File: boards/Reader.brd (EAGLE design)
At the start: 107.6 x 88.9 mm, 46 parts, among them IC1 PIC18F4550_40, T1 BC547, T2 BC547, T3 BC547, X3 PN61729-S

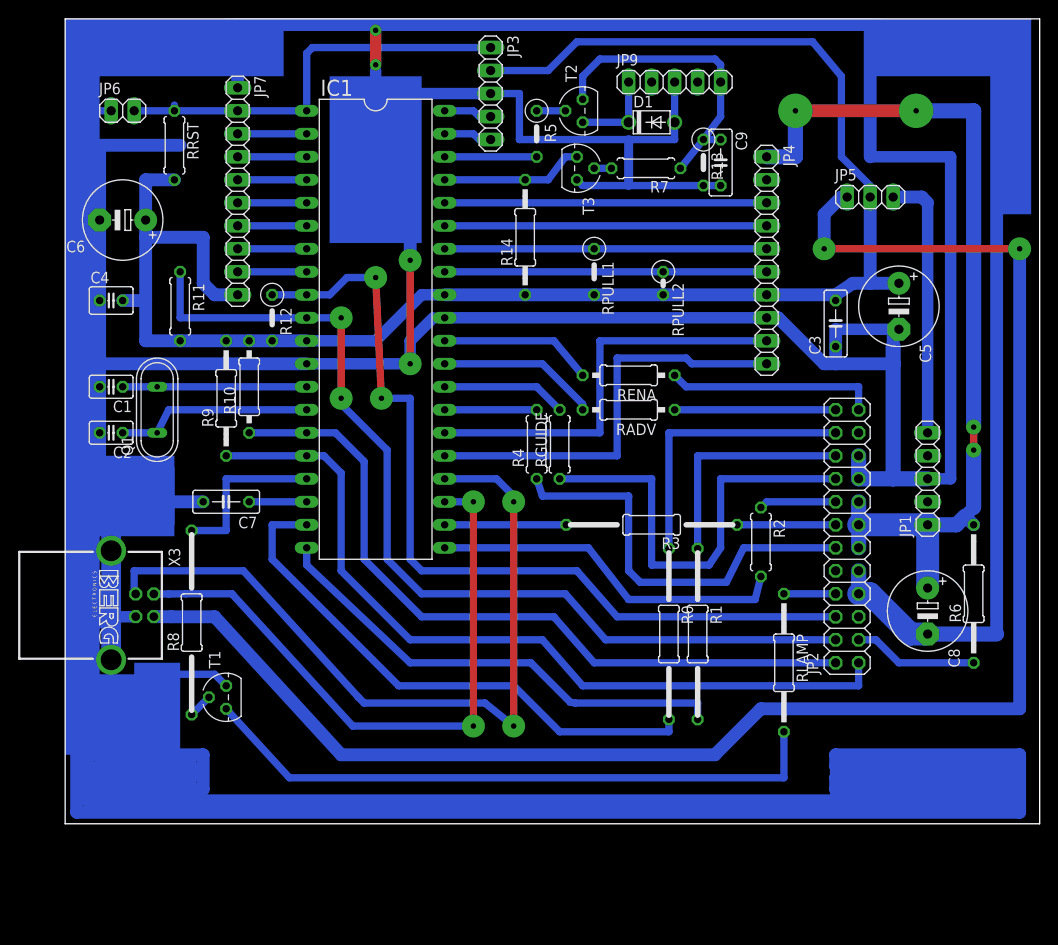
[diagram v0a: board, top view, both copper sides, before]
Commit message: Reader: Added new service
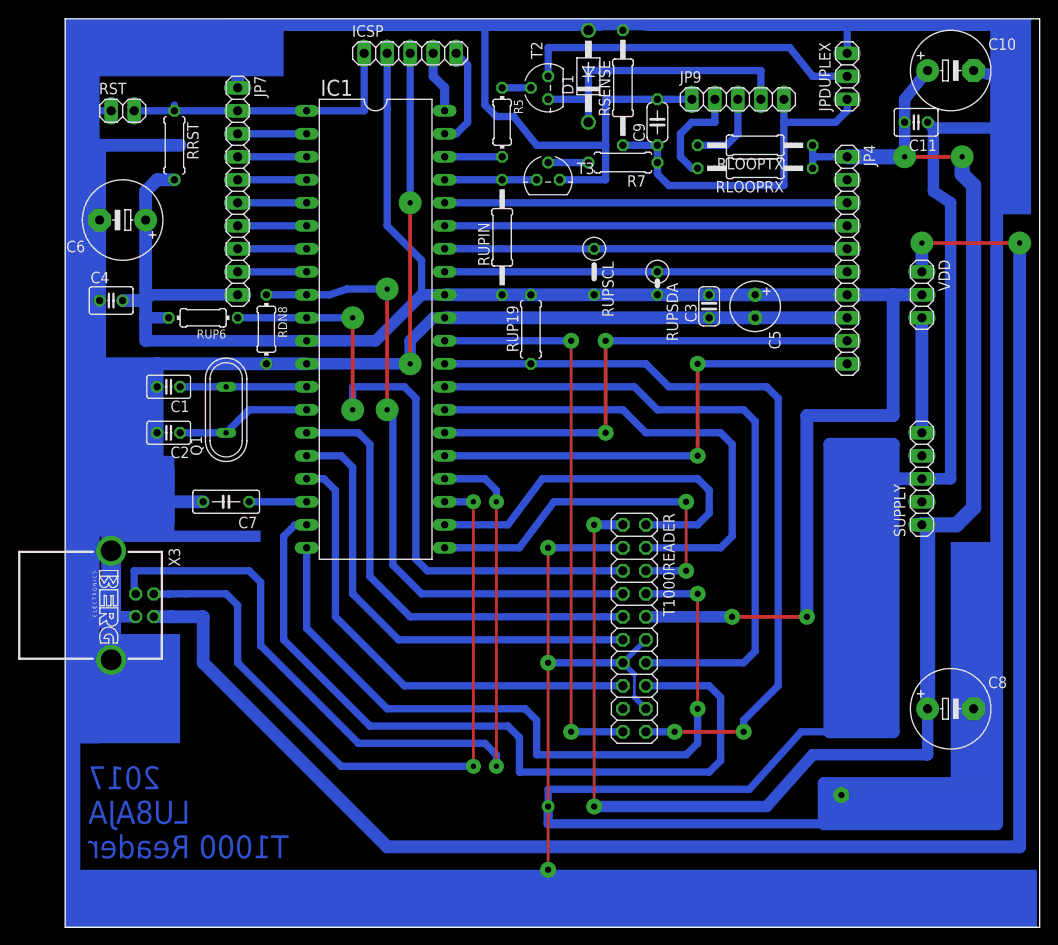
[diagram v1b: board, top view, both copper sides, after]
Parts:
- removed JP1, JP3: (no value), pinhead:1X05
- removed JP2: (no value), pinhead:2X12
- removed JP5: (no value), pinhead:1X03
- removed R0, R1, R3: R-EU0207/19, custom:0207/19
- removed R10, RADV, RENA: R-EU0207/10, custom:0207/10
- removed R11, R2, R4, RGUIDE: R-EU0207/7, custom:0207/7
- removed R12, R13: R-EU0207/5V, custom:0207/5V
- removed R14, R9: R-EU0207/12, custom:0207/12
- removed R6, RLAMP: R-EU0207/15, custom:0207/15
- removed R8: R-EU0207/20, custom:0207/20
- removed RPULL2: R-EU0207/2V, custom:0207/2V
- removed T1: BC547, transistor:TO92
- added C10: (no value), custom:E5-8,5
- added C11: (no value), custom:C025-030X050
- added ICSP, SUPPLY: (no value), pinhead:1X05
- added JPDUPLEX, VDD: (no value), pinhead:1X03
- added RDN8, RUP6: R-EU0204/7, custom:0204/7
- added RLOOPRX, RLOOPTX, RSENSE, RUPIN: R-EU0207/12, custom:0207/12
- added RUP19: R-EU0207/7, custom:0207/7
- added RUPSDA: R-EU0207/2V, custom:0207/2V
- added T1000READER: (no value), pinhead:2X10
- C3: device rcl:C050-025X075 -> custom:C025-024X044
- C5: device rcl:E5-8,5 -> custom:E2,5-6
- C9: device custom:C050-025X075 -> custom:C050-024X044
- D1: value DIODEDO41-05 -> DIODEDO41-10; device custom:DO41-05 -> custom:DO41-10
- JP9: value (none) -> RJ11
- R5: value R-EU0207/5V -> R-EU0204/7; device custom:0207/5V -> custom:0204/7
- moved C5 15.9 mm to (77.5, 47.0)
- moved C3 14.1 mm to (72.4, 47.0)
- moved C8 11.1 mm to (99.1, 2.54), turned to 0 degrees
- moved JP4 8.89 mm to (87.6, 52.1)
- moved D1 8.64 mm to (59.1, 72.4), turned to 90 degrees
- moved C9 8.28 mm to (66.7, 67.3), turned to 90 degrees
- moved Q1 7.62 mm to (19.1, 35.6)
- moved JP9 7.24 mm to (75.6, 69.8)
- moved C1 6.35 mm to (12.7, 38.1)
- moved C2 6.35 mm to (12.7, 33.0)
- moved T2 4.58 mm to (54.6, 71.1)
- moved R5 4.02 mm to (49.5, 67.3)
- moved T3 3.42 mm to (54.6, 61.0), turned to 0 degrees
- moved R7 2.62 mm to (62.9, 62.9)
- renumbered JP6 to RST, RPULL1 to RUPSCL
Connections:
- removed net N$16: JP2.22, R0.1
- removed net N$33: IC1.21, R2.2
- removed net N$36: IC1.19, R0.2
- removed net N$41: JP2.8, RLAMP.1
- removed net N$42: JP2.3, R6.1
- removed net N$43: RLAMP.2, T1.3
- removed net N$44: R8.1, T1.2
- removed net N$7: IC1.10, JP2.4, R11.1
- removed net N$8: IC1.9, JP2.6, R12.1
- net +24V: now also C10.+, C11.2, RLOOPRX.1, RLOOPTX.1, SUPPLY.1, T1000READER.1; no longer JP1.1, JP2.11, JP2.13, JP2.15, R6.2
- net +5V: now also ICSP.2, RUP19.2, RUP6.2, RUPIN.1, RUPSDA.2, T1000READER.10, VDD.2; no longer JP3.2, JP5.2, R10.2, R11.2, R12.2, R14.1, R9.2, RPULL2.2
- net +UB: now also VDD.1; no longer JP5.1
- net GND: now also C10.-, C11.1, D1.A, ICSP.3, JP9.1, JPDUPLEX.3, RDN8.2, RSENSE.2, SUPPLY.3, T1000READER.12, T1000READER.13, T1000READER.18, T1000READER.3; no longer JP1.3, JP2.17, JP2.19, JP2.7, JP2.9, JP3.3, JP9.3, R13.2, T1.1
- net N$1: now also IC1.21, T1000READER.6; no longer JP2.24, RADV.1
- net N$17: now also JP9.3, RLOOPTX.2; no longer IC1.22, R3.2
- net N$18: now also JPDUPLEX.2, T2.1; no longer JP2.20, R1.1
- net N$19: now also JP9.2, RLOOPRX.2; no longer JP2.18, RGUIDE.1
- net N$20: now also IC1.27, T1000READER.4; no longer JP2.16, R2.1
- net N$21: now also IC1.22, T1000READER.2; no longer JP2.14, R3.1
- net N$22: now also IC1.17, T1000READER.15; no longer JP2.12, R4.1
- net N$23: now also IC1.16, T1000READER.11; no longer JP2.23, RENA.1
- net N$24: now also T1000READER.19; no longer RENA.2
- net N$25: now also RUP19.1, T1000READER.20; no longer RADV.2
- net N$26: now also T1000READER.14; no longer RGUIDE.2
- net N$3: now also ICSP.1; no longer JP3.1
- net N$31: now also RUPSDA.1; no longer RPULL2.1
- net N$32: now also IC1.19, T1000READER.16; no longer IC1.27, R4.2
- net N$35: now also T1000READER.8; no longer R1.2
- net N$4: now also IC1.15, T1000READER.9; no longer IC1.17, R8.2
- net N$47: now also RUPIN.2; no longer R14.2
- net N$5: now also IC1.10, RUP6.1, T1000READER.5; no longer IC1.16, JP2.1, R9.1
- net N$50: now also JP9.4; no longer JP9.1
- net N$53: now also ICSP.5; no longer JP3.5
- net N$54: now also ICSP.4; no longer JP3.4
- net N$56: now also JPDUPLEX.1, RSENSE.1; no longer R13.1, T2.1
- net N$6: now also IC1.9, RDN8.1, T1000READER.7; no longer IC1.15, JP2.2, R10.1
- net VCC: now also SUPPLY.5, VDD.3; no longer JP1.5, JP5.3
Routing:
- net N$29: track 361.2 -> 0.00 mm
- net GND: track 587.9 -> 848.9 mm, vias 2 -> 7
- net N$7: track 105.0 -> 0.00 mm, vias 2 -> 0
- net N$8: track 96.3 -> 0.00 mm, vias 2 -> 0
- net N$32: track 10.2 -> 87.3 mm
- net +24V: track 98.7 -> 175.0 mm
- net N$43: track 70.0 -> 0.00 mm
- net N$25: track 17.7 -> 87.6 mm, vias 0 -> 2
- net N$36: track 60.7 -> 0.00 mm
- net N$26: track 13.8 -> 73.9 mm
- net N$24: track 17.0 -> 62.9 mm, vias 0 -> 2
- net N$20: track 8.52 -> 53.5 mm
- net N$33: track 39.7 -> 0.00 mm
- net N$19: track 48.6 -> 11.8 mm
- net N$4: track 18.4 -> 51.9 mm
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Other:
- board size 107.6 x 88.9 mm -> 107.6 x 100.3 mm
- board text added: "2017 LU8AJA T1000 Reader"
